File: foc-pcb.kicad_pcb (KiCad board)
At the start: 4 copper layers, 32 x 32 mm, 88 parts, among them IC1 THVD2450VDRCR, Q1 CSD18540Q5B, Q2 CSD18540Q5B, Q7 CSD18540Q5B, Q8 CSD18540Q5B, U1 UCC272847, U10 TPS63070, U12 C2901617, U17 DF52-4S-0.8H(21), U18 DF52-4S-0.8H(21)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

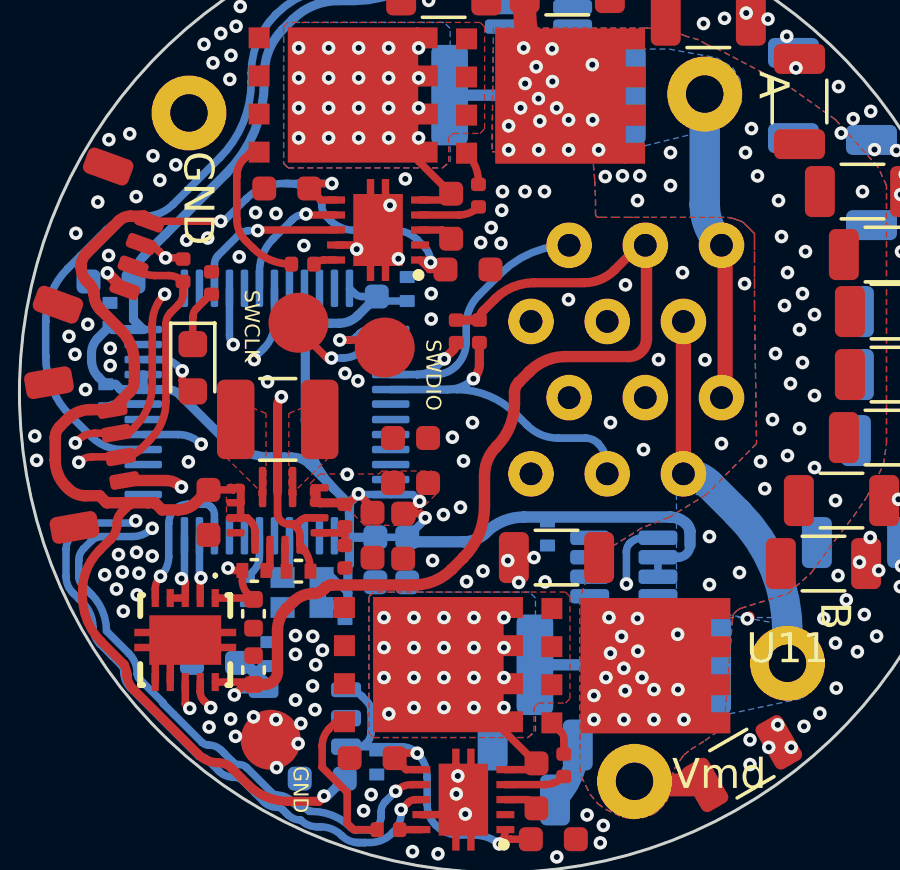
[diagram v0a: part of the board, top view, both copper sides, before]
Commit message: switch to 5V excitation for halls which is confirmed working on hardware
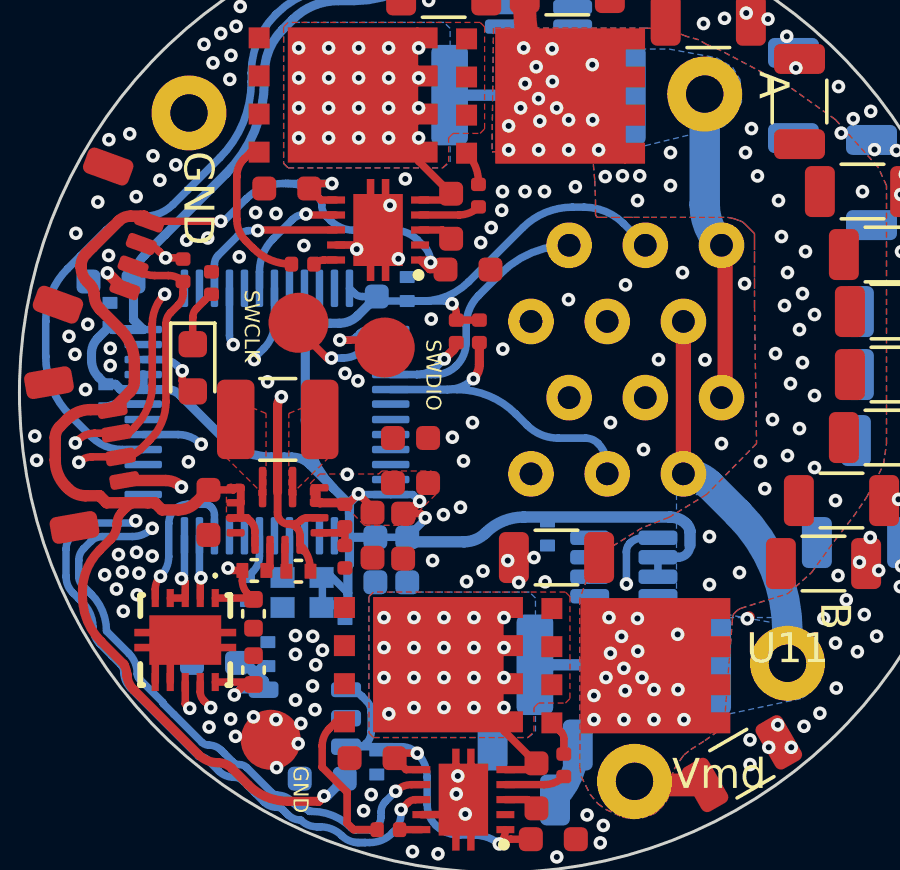
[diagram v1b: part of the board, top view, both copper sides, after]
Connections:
- R5 pad 1: /+5V0 -> +3V3
- R6 pad 1: /+5V0 -> +3V3
- U5 pad 3A: /+5V0 -> +3V3
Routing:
- net /+5V0: track 36.2 -> 5.06 mm
- net +3V3: track 89.0 -> 101.4 mm, vias 4 -> 5
